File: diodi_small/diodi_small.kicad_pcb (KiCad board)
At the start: 2 copper layers, 26.7 x 29.2 mm, 14 parts

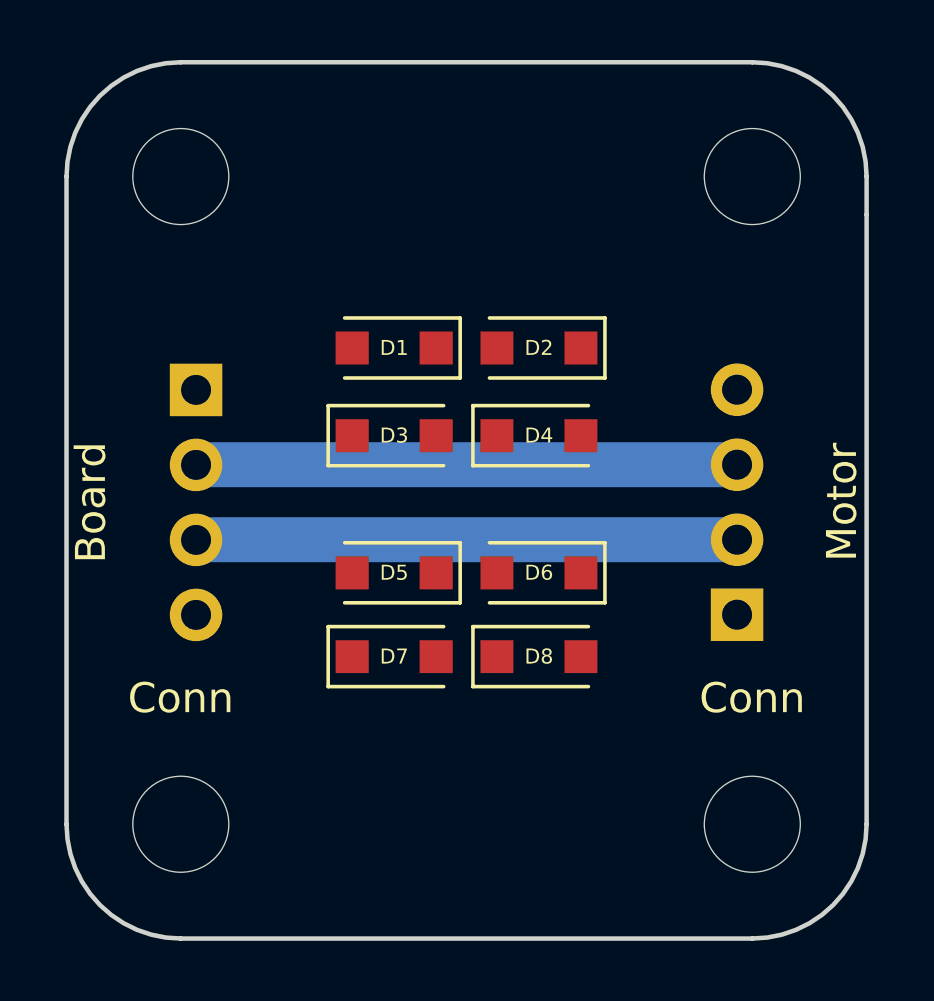
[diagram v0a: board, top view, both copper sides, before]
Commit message: Add files via upload
New traces and updated labels
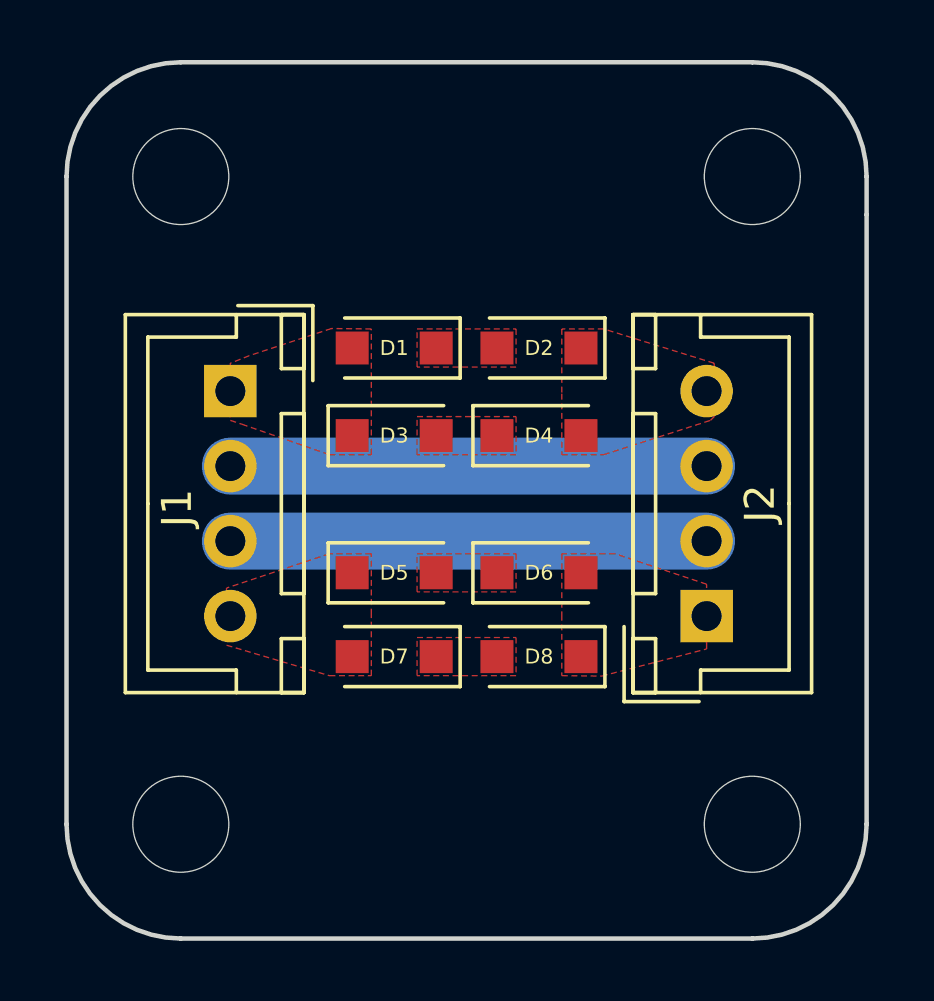
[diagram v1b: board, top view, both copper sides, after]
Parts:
- removed Board, Motor: CONN_01X04, Connectors_JST:JST_XH_B04B-XH-A_04x2.50mm_Straight
- added J1: CONN_01X04, Connectors_JST:JST_XH_B04B-XH-A_04x2.50mm_Straight, F.Cu at (131.2, 64.3)
- added J2: CONN_01X04, Connectors_JST:JST_XH_B04B-XH-A_04x2.50mm_Straight, F.Cu at (147.1, 71.8)
- turned D5 to 0 degrees
- turned D6 to 0 degrees
- turned D7 to 180 degrees
- turned D8 to 180 degrees
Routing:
- net Net-(J1-Pad3): track 18.0 -> 15.9 mm
- net Net-(J1-Pad2): track 18.0 -> 15.9 mm
- added copper zone on F.Cu, net Net-(D1-Pad1)
- added copper zone on F.Cu, net Net-(D1-Pad2)
- added copper zone on F.Cu, net Net-(D2-Pad1)
- added copper zone on F.Cu, net Net-(D3-Pad2)
- added copper zone on F.Cu, net Net-(D5-Pad1)
- added copper zone on F.Cu, net Net-(D5-Pad2)
- added copper zone on F.Cu, net Net-(D6-Pad2)
- added copper zone on F.Cu, net Net-(D7-Pad1)
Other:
- rule pad_to_mask_clearance: 0.2 -> 0.1

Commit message: Add files via upload
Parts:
- added G***: LOGO, graphics:adictiverseq, F.Cu at (139.1, 79.3)
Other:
- board text added: "Stepper motor lifeguard V2"
- board text added: "«In the twenty-first century, the robot will take the place which slave labor occupied in ancient civilization.» Nikola Tesla"
